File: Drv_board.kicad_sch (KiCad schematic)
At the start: 0 parts

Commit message: working on power
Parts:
- added BT1: Battery, TerminalBlock_Phoenix:TerminalBlock_Phoenix_MKDS-1,5-2-5.08_1x02_P5.08mm_Horizontal, symbol Device:Battery
- added C1: 1u, symbol Device:C_Small
- added C2: 3n3, symbol Device:C_Small
- added C3, C9: 100n, symbol Device:C_Small
- added C4, C5: 22u, symbol Device:C_Small
- added C6, C7: 10u, symbol Device:C_Small
- added C8: 5-22p, symbol Device:C_Small
- added IC1: TPS54228D, SOIC127P600X175-8N, symbol TPS54228D:TPS54228D
- added L1: 4u7 2.5 A, symbol Device:L_Small
- added R1: 10k, symbol Device:R_Small
- added R2: 165k, symbol Device:R_Small
- added R3: 22k1, symbol Device:R_Small
- added U1: LD1117S50, Package_TO_SOT_SMD:SOT-223-3_TabPin2, symbol Regulator_Linear:LD1117S50TR_SOT223
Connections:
- new net: IC1.1 (EN), R1.1
- new net: C8.1, IC1.2 (VFB), R2.1, R3.2
- new net: C3.2, IC1.6 (SW), L1.1
- new net: C1.1, IC1.3 (VREG5)
- new net: C2.1, IC1.4 (SS)
- new net: C3.1, IC1.7 (VBST)
- new net +6V: C4.1, C5.1, C8.2, C9.1, L1.2, R2.2, U1.3 (VI)
- new net +BATT: BT1.1 (+), C6.1, C7.1, IC1.8 (VIN)
- new net -BATT: BT1.2 (-), C1.2, C2.2, C4.2, C5.2, C6.2, C7.2, C9.2, IC1.5 (GND), R3.1, U1.1 (GND)
- new net 6V_EN: R1.2
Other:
- note added: "2x 18650 Li-ion (3.2 - 8.4 V)"

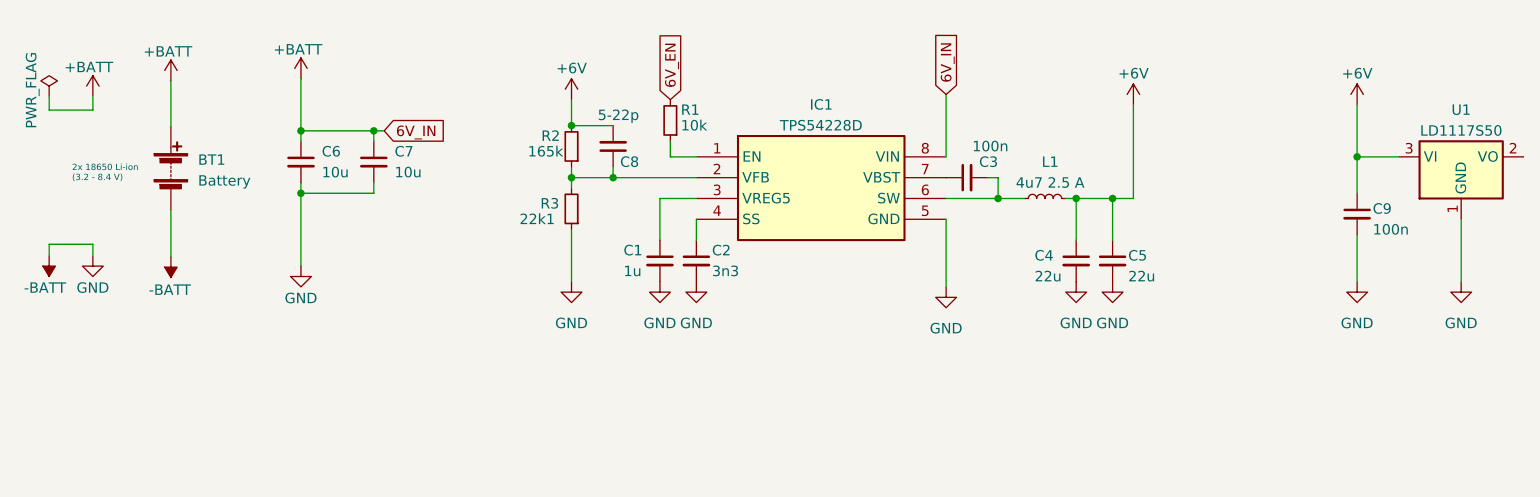
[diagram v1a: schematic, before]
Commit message: Added power supply and motor schematics
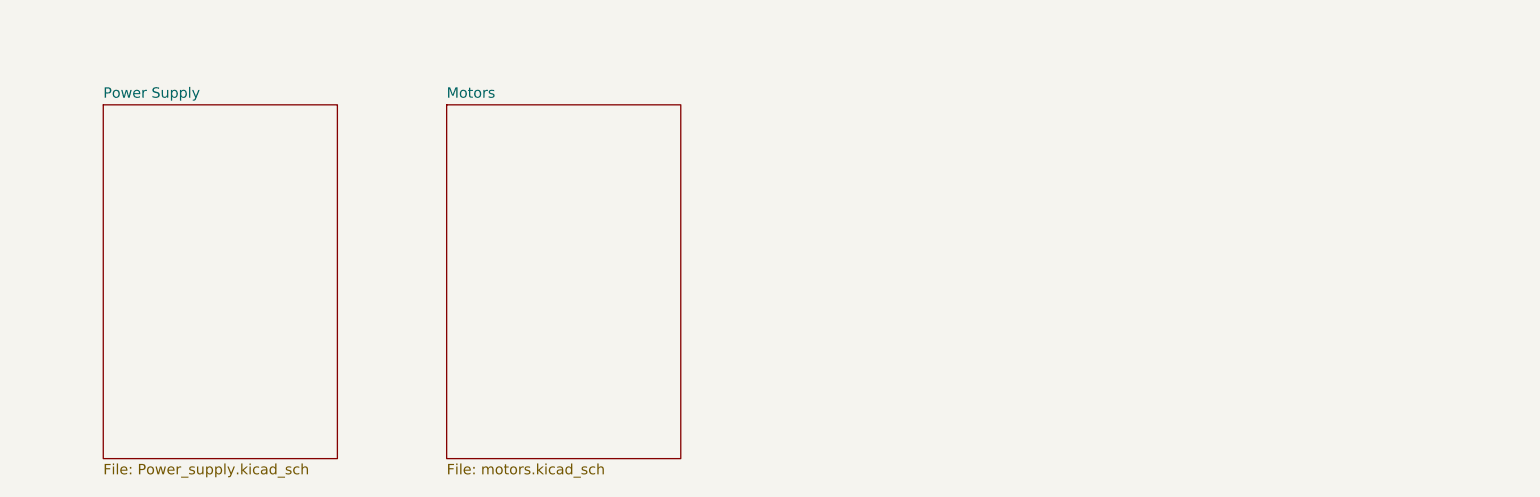
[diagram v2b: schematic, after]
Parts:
- removed BT1: Battery, TerminalBlock_Phoenix:TerminalBlock_Phoenix_MKDS-1,5-2-5.08_1x02_P5.08mm_Horizontal, symbol Device:Battery
- removed C1: 1u, symbol Device:C_Small
- removed C2: 3n3, symbol Device:C_Small
- removed C3, C9: 100n, symbol Device:C_Small
- removed C4, C5: 22u, symbol Device:C_Small
- removed C6, C7: 10u, symbol Device:C_Small
- removed C8: 5-22p, symbol Device:C_Small
- removed IC1: TPS54228D, SOIC127P600X175-8N, symbol TPS54228D:TPS54228D
- removed L1: 4u7 2.5 A, symbol Device:L_Small
- removed R1: 10k, symbol Device:R_Small
- removed R2: 165k, symbol Device:R_Small
- removed R3: 22k1, symbol Device:R_Small
- removed U1: LD1117S50, Package_TO_SOT_SMD:SOT-223-3_TabPin2, symbol Regulator_Linear:LD1117S50TR_SOT223
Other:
- added sheet Motors (motors.kicad_sch)
- added sheet Power Supply (Power_supply.kicad_sch)
- note removed: "2x 18650 Li-ion (3.2 - 8.4 V)"

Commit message: work progress
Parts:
- added C10, C6, C7, C8 (x2), C9: 100n, Capacitor_SMD:C_0603_1608Metric, symbol Device:C_Small
- added C13, C14: 10p, Capacitor_SMD:C_0402_1005Metric, symbol Device:C_Small
- added C5: 4u7, Capacitor_SMD:C_0603_1608Metric, symbol Device:C_Small
- added C8 (x2): 1u, Capacitor_SMD:C_0603_1608Metric, symbol Device:C_Small
- added C8: 10n, Capacitor_SMD:C_0603_1608Metric, symbol Device:C_Small
- added FB1: 120R, symbol Device:FerriteBead_Small
- added R4: 10k, Resistor_SMD:R_0603_1608Metric, symbol Device:R_Small
- added R7: 10k, Resistor_SMD:R_0603_1608Metric, symbol Device:R
- added S2: RESET, digikey-footprints:PushButton_12x12mm_THT_GPTS203211B, symbol dk_Pushbutton-Switches:GPTS203211B
- added SW1: SW_SPDT, Jumper:SolderJumper-3_P1.3mm_Open_RoundedPad1.0x1.5mm, symbol Switch:SW_SPDT
- added U7: STM32F107RCTx, Package_QFP:LQFP-64_10x10mm_P0.5mm, symbol MCU_ST_STM32F1:STM32F107RCTx
- added Y3: 16 MHz, Crystal:Crystal_SMD_3225-4Pin_3.2x2.5mm, symbol Device:Crystal_GND24_Small
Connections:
- new net: C14.1, U7.6 (PD1), Y3.3
- new net: C13.1, U7.5 (PD0), Y3.1
- new net: C8.1, R4.2, S2.2, U7.7 (NRST)
- new net: R7.2, SW1.2 (B)
- new net +3.3V: C10.1, C5.1, C6.1, C7.1, C8.1, C8.1, C9.1, FB1.2, R4.1, SW1.1 (A), U7.1 (VBAT), U7.19 (VDD), U7.32 (VDD), U7.48 (VDD), U7.64 (VDD)
- new net +3.3VA: C8.1, C8.1, FB1.1, U7.13 (VDDA)
- new net BOOT0: R7.1, U7.60 (BOOT0)
- new net DRV_MODE: U7.2 (PC13)
- new net DRV_NSLEEP: U7.3 (PC14)
- new net GND: C10.2, C13.2, C14.2, C5.2, C6.2, C7.2, C8.2, C8.2, C8.2, C8.2, C8.2, C9.2, S2.1, SW1.3 (C), U7.12 (VSSA), U7.18 (VSS), U7.31 (VSS), U7.47 (VSS), U7.63 (VSS), Y3.2, Y3.4
- new net I2C_SCL: U7.61 (PB8)
- new net I2C_SDA: U7.62 (PB9)
- new net MPU-6050_IRQ: U7.57 (PB5)
- new net NRF_CE: U7.56 (PB4)
- new net NRF_CSN: U7.54 (PD2)
- new net NRF_IRQ: U7.50 (PA15)
- new net NRF_MISO: U7.52 (PC11)
- new net NRF_MOSI: U7.53 (PC12)
- new net NRF_SCK: U7.51 (PC10)
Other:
- added sheet Peripherals (peripherals.kicad_sch)
- note added: "Cload = 2 * (CL - Cstray[6])"
- note added: "Place them close to uC!"
- note added: "uC Decoupling"

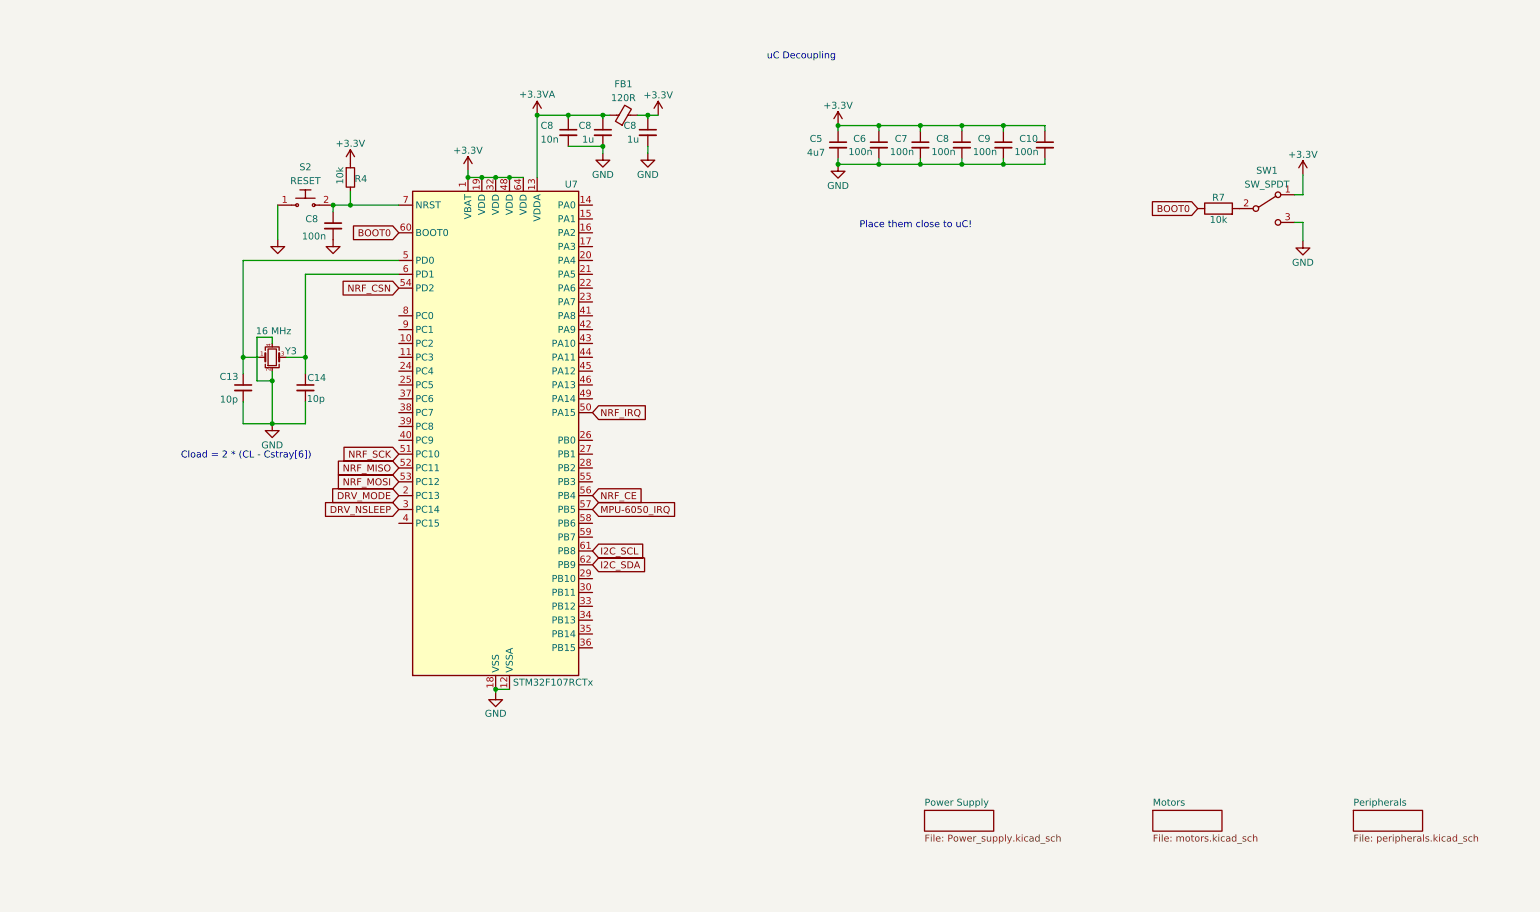
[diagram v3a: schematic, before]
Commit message: most of the components added
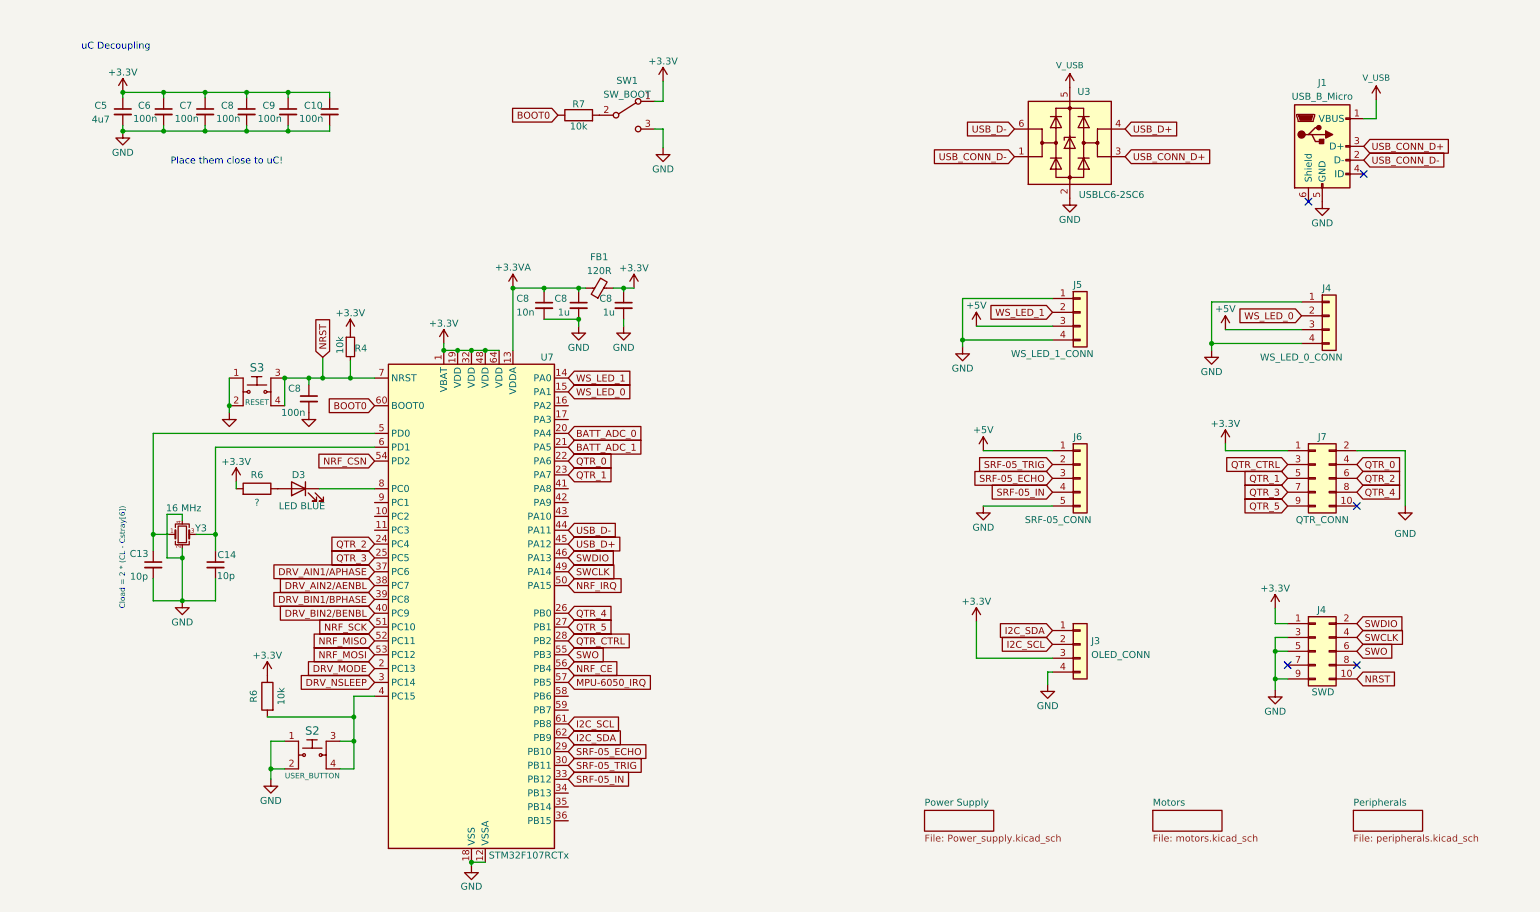
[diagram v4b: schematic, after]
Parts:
- removed S2: RESET, digikey-footprints:PushButton_12x12mm_THT_GPTS203211B, symbol dk_Pushbutton-Switches:GPTS203211B
- added D3: LED BLUE, LED_SMD:LED_0805_2012Metric, symbol Device:LED
- added J1: USB_B_Micro, Connector_USB:USB_Micro-B_Amphenol_10103594-0001LF_Horizontal, symbol Connector:USB_B_Micro
- added J3: OLED_CONN, Connector_PinHeader_2.54mm:PinHeader_1x04_P2.54mm_Vertical, symbol Connector_Generic:Conn_01x04
- added J4: SWD, Connector_PinHeader_2.54mm:PinHeader_2x05_P2.54mm_Vertical, symbol Connector_Generic:Conn_02x05_Odd_Even
- added J4: WS_LED_0_CONN, symbol Connector_Generic:Conn_01x04
- added J5: WS_LED_1_CONN, symbol Connector_Generic:Conn_01x04
- added J6: SRF-05_CONN, symbol Connector_Generic:Conn_01x05
- added J7: QTR_CONN, symbol Connector_Generic:Conn_02x05_Odd_Even
- added R6: ?, Resistor_SMD:R_0603_1608Metric, symbol Device:R
- added R6: 10k, Resistor_SMD:R_0603_1608Metric, symbol Device:R
- added S2: USER_BUTTON, Button_Switch_SMD:SW_MEC_5GSH9, symbol dk_Tactile-Switches:1825910-6
- added S3: RESET, Button_Switch_SMD:SW_MEC_5GSH9, symbol dk_Tactile-Switches:1825910-6
- added U3: USBLC6-2SC6, Package_TO_SOT_SMD:SOT-23-6, symbol Power_Protection:USBLC6-2SC6
- SW1: value SW_SPDT -> SW_BOOT
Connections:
- net +3.3V: now also J3.3 (Pin_3), J4.1 (Pin_1), J7.1 (Pin_1), R6.1, R6.2
- net GND: now also J1.5 (GND), J3.4 (Pin_4), J4.1 (Pin_1), J4.3 (Pin_3), J4.4 (Pin_4), J4.5 (Pin_5), J4.9 (Pin_9), J5.1 (Pin_1), J5.4 (Pin_4), J6.5 (Pin_5), J7.2 (Pin_2), S2.1, S2.2, S3.1, S3.2, U3.2 (GND)
- net I2C_SCL: now also J3.2 (Pin_2)
- net I2C_SDA: now also J3.1 (Pin_1)
- net WS_LED_1: now reaches U7.14 (PA0)
- net WS_LED_1: now also J5.2 (Pin_2)
- net WS_LED_0: now reaches U7.15 (PA1)
- net WS_LED_0: now also J4.2 (Pin_2)
- net BATT_ADC_0: now reaches U7.20 (PA4)
- net BATT_ADC_1: now reaches U7.21 (PA5)
- net QTR_0: now reaches U7.22 (PA6)
- net QTR_0: now also J7.4 (Pin_4)
- net QTR_1: now reaches U7.23 (PA7)
- net QTR_1: now also J7.5 (Pin_5)
- net QTR_2: now reaches U7.24 (PC4)
- net QTR_2: now also J7.6 (Pin_6)
- net QTR_3: now reaches U7.25 (PC5)
- net QTR_3: now also J7.7 (Pin_7)
- net QTR_4: now reaches U7.26 (PB0)
- net QTR_4: now also J7.8 (Pin_8)
- net QTR_5: now reaches U7.27 (PB1)
- net QTR_5: now also J7.9 (Pin_9)
- net QTR_CTRL: now reaches U7.28 (PB2)
- net QTR_CTRL: now also J7.3 (Pin_3)
- net SRF-05_ECHO: now reaches U7.29 (PB10)
- net SRF-05_ECHO: now also J6.3 (Pin_3)
- net SRF-05_TRIG: now reaches U7.30 (PB11)
- net SRF-05_TRIG: now also J6.2 (Pin_2)
- net SRF-05_IN: now reaches U7.33 (PB12)
- net SRF-05_IN: now also J6.4 (Pin_4)
- net DRV_AIN1/APHASE: now reaches U7.37 (PC6)
- net DRV_AIN2/AENBL: now reaches U7.38 (PC7)
- net DRV_BIN1/BPHASE: now reaches U7.39 (PC8)
- net at U7.4 (PC15): now also R6.2, S2.3, S2.4
- net DRV_BIN2/BENBL: now reaches U7.40 (PC9)
- net USB_D-: now reaches U7.44 (PA11)
- net USB_D-: now also U3.6 (I/O1)
- net USB_D+: now reaches U7.45 (PA12)
- net USB_D+: now also U3.4 (I/O2)
- net SWDIO: now reaches U7.46 (PA13)
- net SWDIO: now also J4.2 (Pin_2)
- net SWCLK: now reaches U7.49 (PA14)
- net SWCLK: now also J4.4 (Pin_4)
- net SWO: now reaches U7.55 (PB3)
- net SWO: now also J4.6 (Pin_6)
- net NRST: now reaches C8.1, R4.2, U7.7 (NRST)
- net NRST: now also J4.10 (Pin_10), S3.3, S3.4
- net at U7.8 (PC0): now also D3.1 (K)
- new net: D3.2 (A), R6.1
- new net +5V: J4.3 (Pin_3), J5.3 (Pin_3), J6.1 (Pin_1)
- new net USB_CONN_D+: J1.3 (D+), U3.3 (I/O2)
- new net USB_CONN_D-: J1.2 (D-), U3.1 (I/O1)
- new net V_USB: J1.1 (VBUS), U3.5 (VBUS)
- no-connect marks 0 -> 5
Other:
- moved on the sheet: C10, C13, C14, C5, C6, C7, C8, C9, FB1, R4, R7, SW1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

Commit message: schematic completed
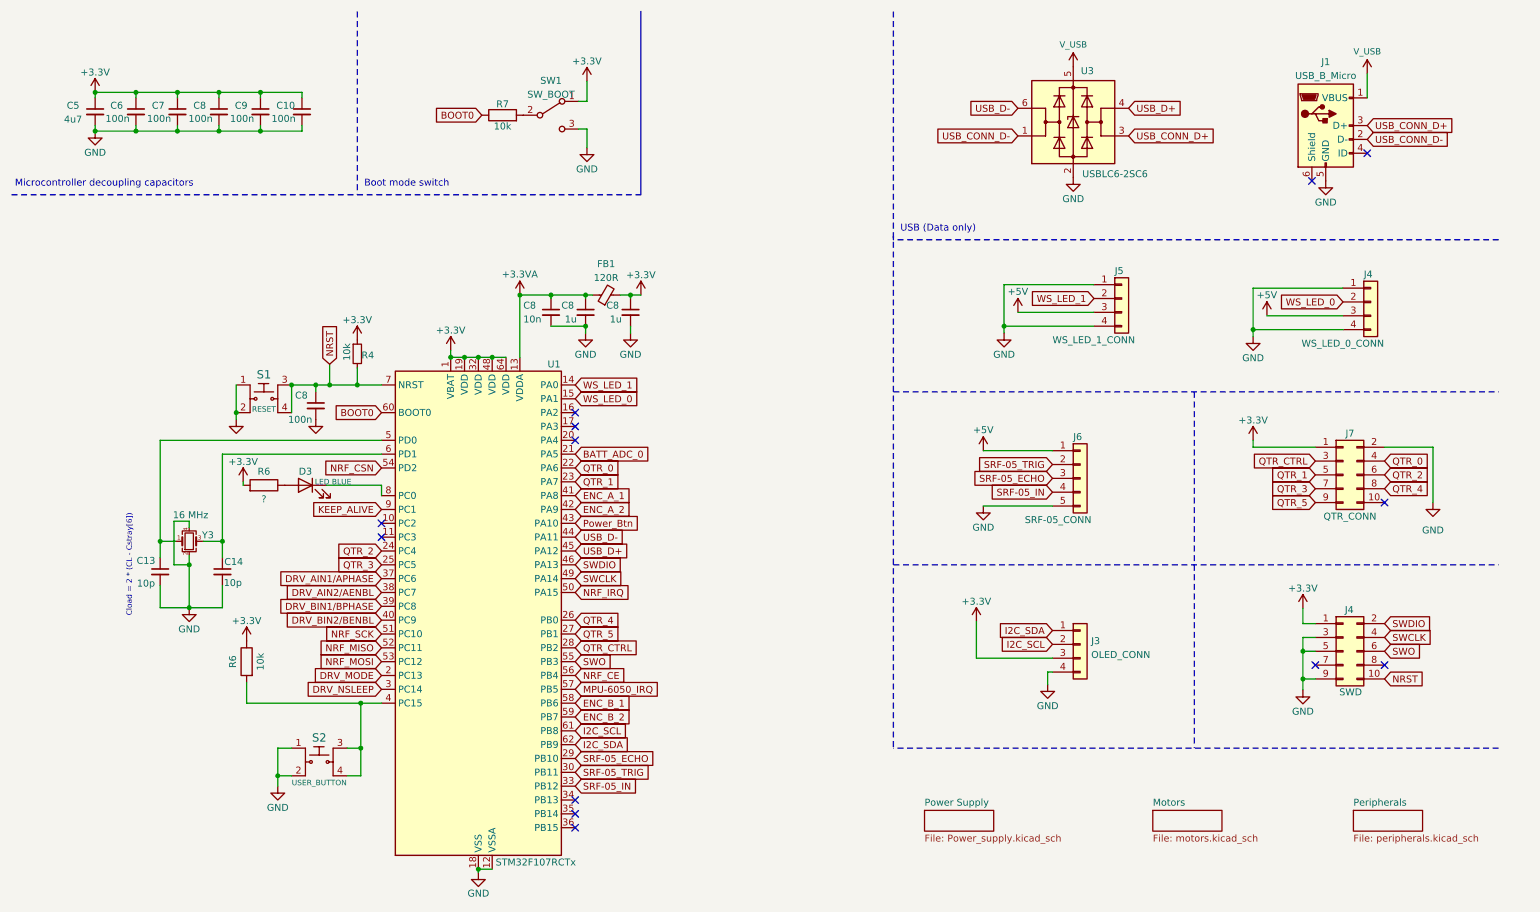
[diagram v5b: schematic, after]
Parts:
- FB1: footprint (none) -> Inductor_SMD:L_0603_1608Metric
- J3: footprint Connector_PinHeader_2.54mm:PinHeader_1x04_P2.54mm_Vertical -> DF3A-4P-2DSA:SHDR4W55P0X200_1X4_1000X500X530P
- J4, J5: footprint (none) -> DF3A-4P-2DSA:SHDR4W55P0X200_1X4_1000X500X530P
- J6: footprint (none) -> DF3A-5P-2DSA:SHDR5W55P0X200_1X5_1200X500X530P
- J7: footprint (none) -> Connector_IDC:IDC-Header_2x05_P2.54mm_Vertical
- S1: renamed from S3; footprint Button_Switch_SMD:SW_MEC_5GSH9 -> TL3305CF160QG:TL3305AF160QG
- S2: footprint Button_Switch_SMD:SW_MEC_5GSH9 -> TL3305CF160QG:TL3305AF160QG
- SW1: footprint Jumper:SolderJumper-3_P1.3mm_Open_RoundedPad1.0x1.5mm -> Connector_PinHeader_1.00mm:PinHeader_1x03_P1.00mm_Vertical
- renumbered U7 to U1
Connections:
- net BATT_ADC_1 is gone; now on net BATT_ADC_0: U1.21 (PA5)
- net BATT_ADC_0: no longer U1.20 (PA4)
- net ENC_A_1: now reaches U1.41 (PA8)
- net ENC_A_2: now reaches U1.42 (PA9)
- net Power_Btn: now reaches U1.43 (PA10)
- net ENC_B_1: now reaches U1.58 (PB6)
- net ENC_B_2: now reaches U1.59 (PB7)
- net KEEP_ALIVE: now reaches U1.9 (PC1)
- no-connect marks 5 -> 13
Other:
- note added: "Boot mode switch"
- note added: "Microcontroller decoupling capacitors"
- note added: "USB (Data only)"
- note removed: "Place them close to uC!"
- note removed: "uC Decoupling"
- moved on the sheet: C10, C13, C14, C5, C6, C7, C8, C9, D3, FB1, J1, J4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

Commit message: done boost converter layout
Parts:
- J4: footprint Connector_PinHeader_2.54mm:PinHeader_2x05_P2.54mm_Vertical -> Connector_PinHeader_2.00mm:PinHeader_2x05_P2.00mm_Vertical
- SW1: footprint Connector_PinHeader_1.00mm:PinHeader_1x03_P1.00mm_Vertical -> Connector_PinHeader_2.54mm:PinHeader_1x03_P2.54mm_Vertical
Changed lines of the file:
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@@
       (effects (font (size 1.27 1.27)))
     )
-    (property "Footprint" "Connector_PinHeader_2.54mm:PinHeader_2x05_P2.54mm_Vertical" (at 256.54 129.54 0)
+    (property "Footprint" "Connector_PinHeader_2.00mm:PinHeader_2x05_P2.00mm_Vertical" (at 256.54 129.54 0)
       (effects (font (size 1.27 1.27)) hide)
     )
@@
       (effects (font (size 1.27 1.27)))
     )
-    (property "Footprint" "Connector_PinHeader_1.00mm:PinHeader_1x03_P1.00mm_Vertical" (at 111.125 31.115 0)
-      (effects (font (size 1.27 1.27)) hide)
-    )
+    (property "Footprint" "Connector_PinHeader_2.54mm:PinHeader_1x03_P2.54mm_Vertical" (at 111.125 31.115 0)
+      (effects (font (size 1.27 1.27)) hide)
+    )

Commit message: working on pcb
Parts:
- removed S1: RESET, TL3305CF160QG:TL3305AF160QG, symbol dk_Tactile-Switches:1825910-6
- removed S2: USER_BUTTON, TL3305CF160QG:TL3305AF160QG, symbol dk_Tactile-Switches:1825910-6
- added S1: RESET, digikey-footprints:Switch_Tactile_SMD_6x6mm_PTS645, symbol dk_Tactile-Switches:PTS645SM43SMTR92_LFS
- added S2: USER_BUTTON, digikey-footprints:Switch_Tactile_SMD_6x6mm_PTS645, symbol dk_Tactile-Switches:PTS645SM43SMTR92_LFS
- C13, C14: footprint Capacitor_SMD:C_0402_1005Metric -> Capacitor_SMD:C_0603_1608Metric
- D3: footprint LED_SMD:LED_0805_2012Metric -> LED_SMD:LED_0603_1608Metric
- SW1: footprint Connector_PinHeader_2.54mm:PinHeader_1x03_P2.54mm_Vertical -> Jumper:SolderJumper-3_P1.3mm_Open_Pad1.0x1.5mm
- renumbered U1 to U2
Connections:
- net GND: now also S1.1, S1.2, S2.1, S2.2
- net NRST: now also S1.3, S1.4
- net at R6.2, U2.4 (PC15): now also S2.3, S2.4
